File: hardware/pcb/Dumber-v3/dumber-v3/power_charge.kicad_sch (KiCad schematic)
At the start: 44 parts, among them P1 USB_C_Plug_GCT_USB4125, Q1 PMN52XP, SW1 SW_Push, U3 LTC2954, U4 L6924U, U5 NCV5171, U6 DIO6010

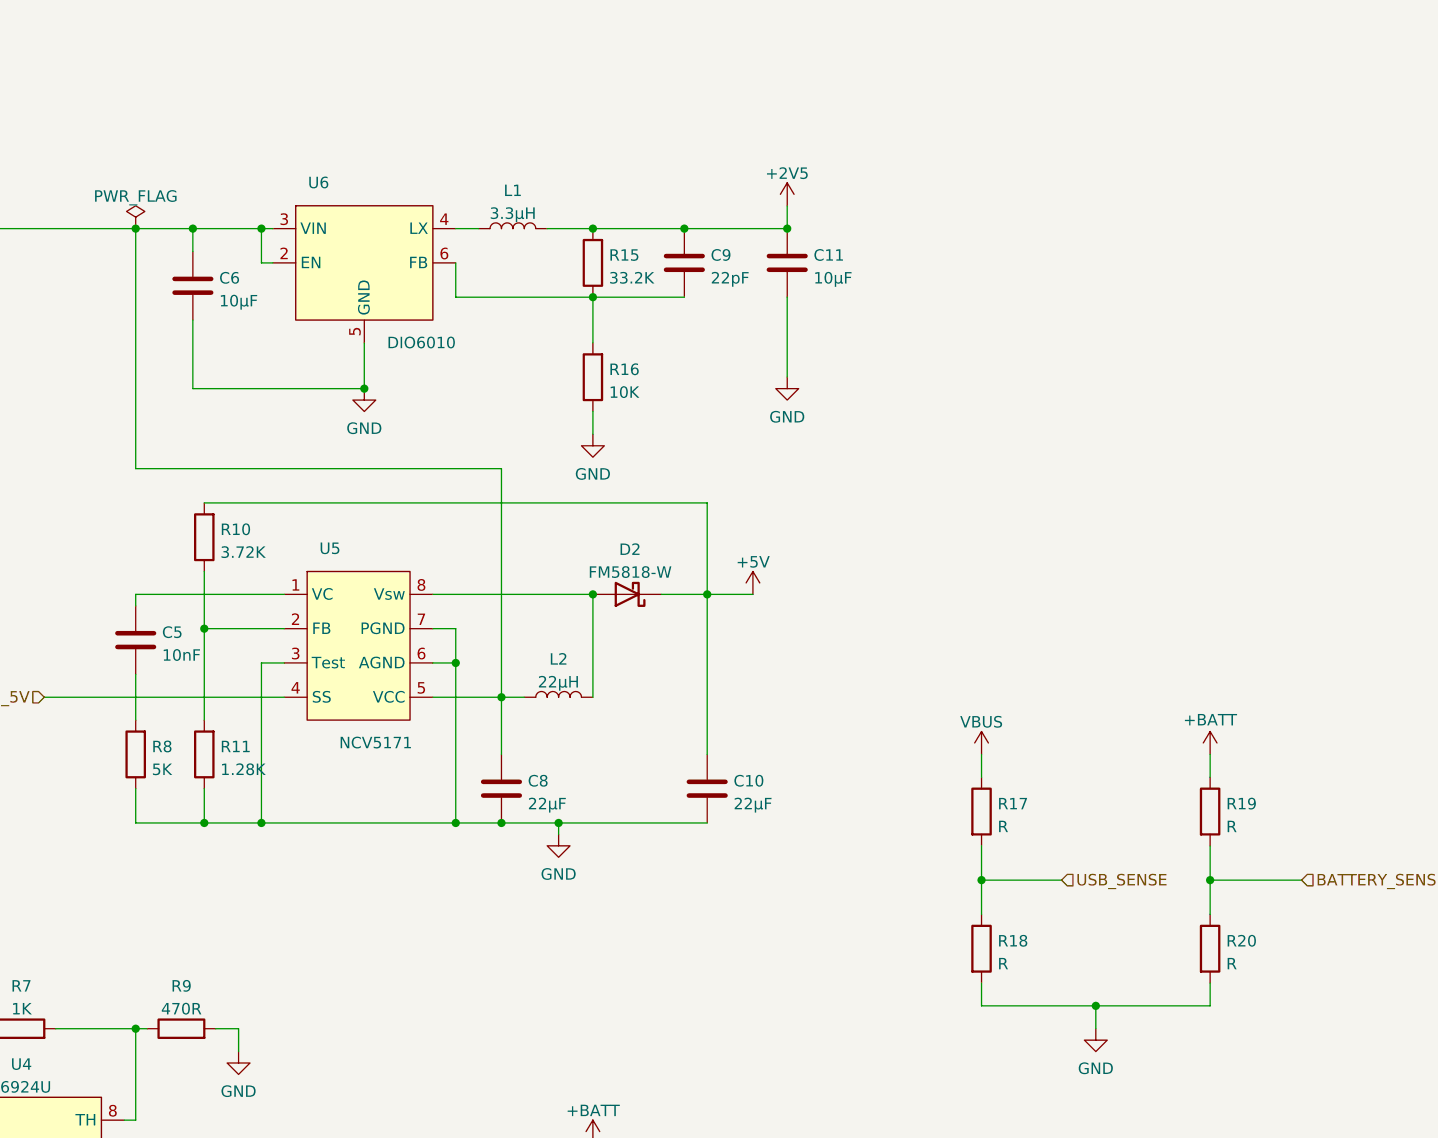
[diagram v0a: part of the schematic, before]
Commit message: Schema complet, projet logiciel demarré
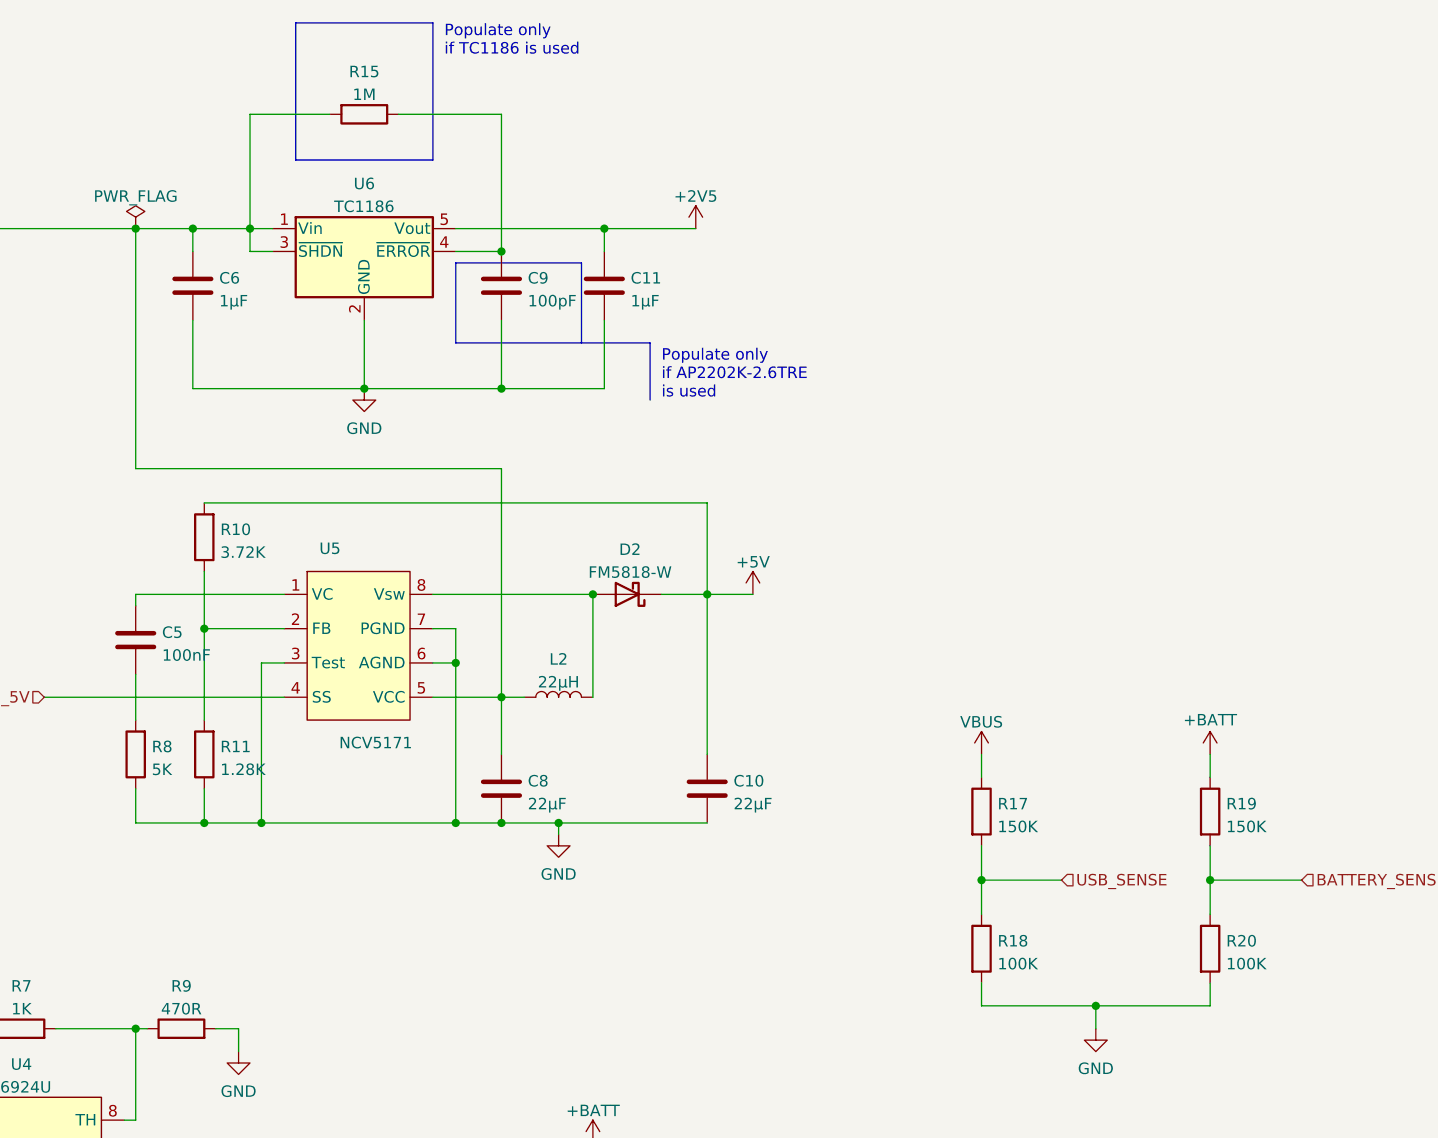
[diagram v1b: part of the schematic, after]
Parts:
- removed L1: 3.3µH, Inductor_SMD:L_Vishay_IHLP-2525, symbol Device:L
- removed R16: 10K, Resistor_SMD:R_0805_2012Metric, symbol Device:R
- removed U6: DIO6010, Package_DFN_QFN:DFN-6-1EP_2x2mm_P0.5mm_EP0.6x1.37mm, symbol Insa:DIO6010
- added U6: TC1186, Package_TO_SOT_SMD:SOT-23-5, symbol Regulator_Linear:TC1186
- C11, C6: value 10µF -> 1µF
- C5: value 10nF -> 100nF
- C9: value 22pF -> 100pF
- L2: footprint Inductor_SMD:L_Vishay_IHLP-4040 -> Inductor_SMD:L_Taiyo-Yuden_MD-4040
- R15: value 33.2K -> 1M
- R17, R19: value R -> 150K
- R18, R20: value R -> 100K
- U4: footprint Package_DFN_QFN:VQFN-16-1EP_3x3mm_P0.5mm_EP1.6x1.6mm_ThermalVias -> INSA:L6924UTR
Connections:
- net +2V5: now also U6.5 (Vout); no longer C9.1, R15.2
- net GND: now also C9.2, U6.2 (GND)
- net at R15.1: now also C9.1, U6.4 (~{ERROR}); no longer C9.2
- net at C6.1, C8.1, D1.3 (A)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: now also R15.2, U6.1 (Vin), U6.3 (~{SHDN})
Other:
- note added: "Populate only if AP2202K-2.6TRE is used"
- note added: "Populate only if TC1186 is used"

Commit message: nouvelle version pcb dumber + nouvelle version monietur en QT
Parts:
- BT1: footprint Battery:BatteryHolder_Keystone_2460_1xAA -> INSA:Battery-14500
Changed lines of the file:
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@@
       (effects (font (size 1.27 1.27)) (justify left))
     )
-    (property "Footprint" "Battery:BatteryHolder_Keystone_2460_1xAA" (id 2) (at 171.45 152.146 90)
+    (property "Footprint" "INSA:Battery-14500" (id 2) (at 171.45 152.146 90)
       (effects (font (size 1.27 1.27)) hide)
     )

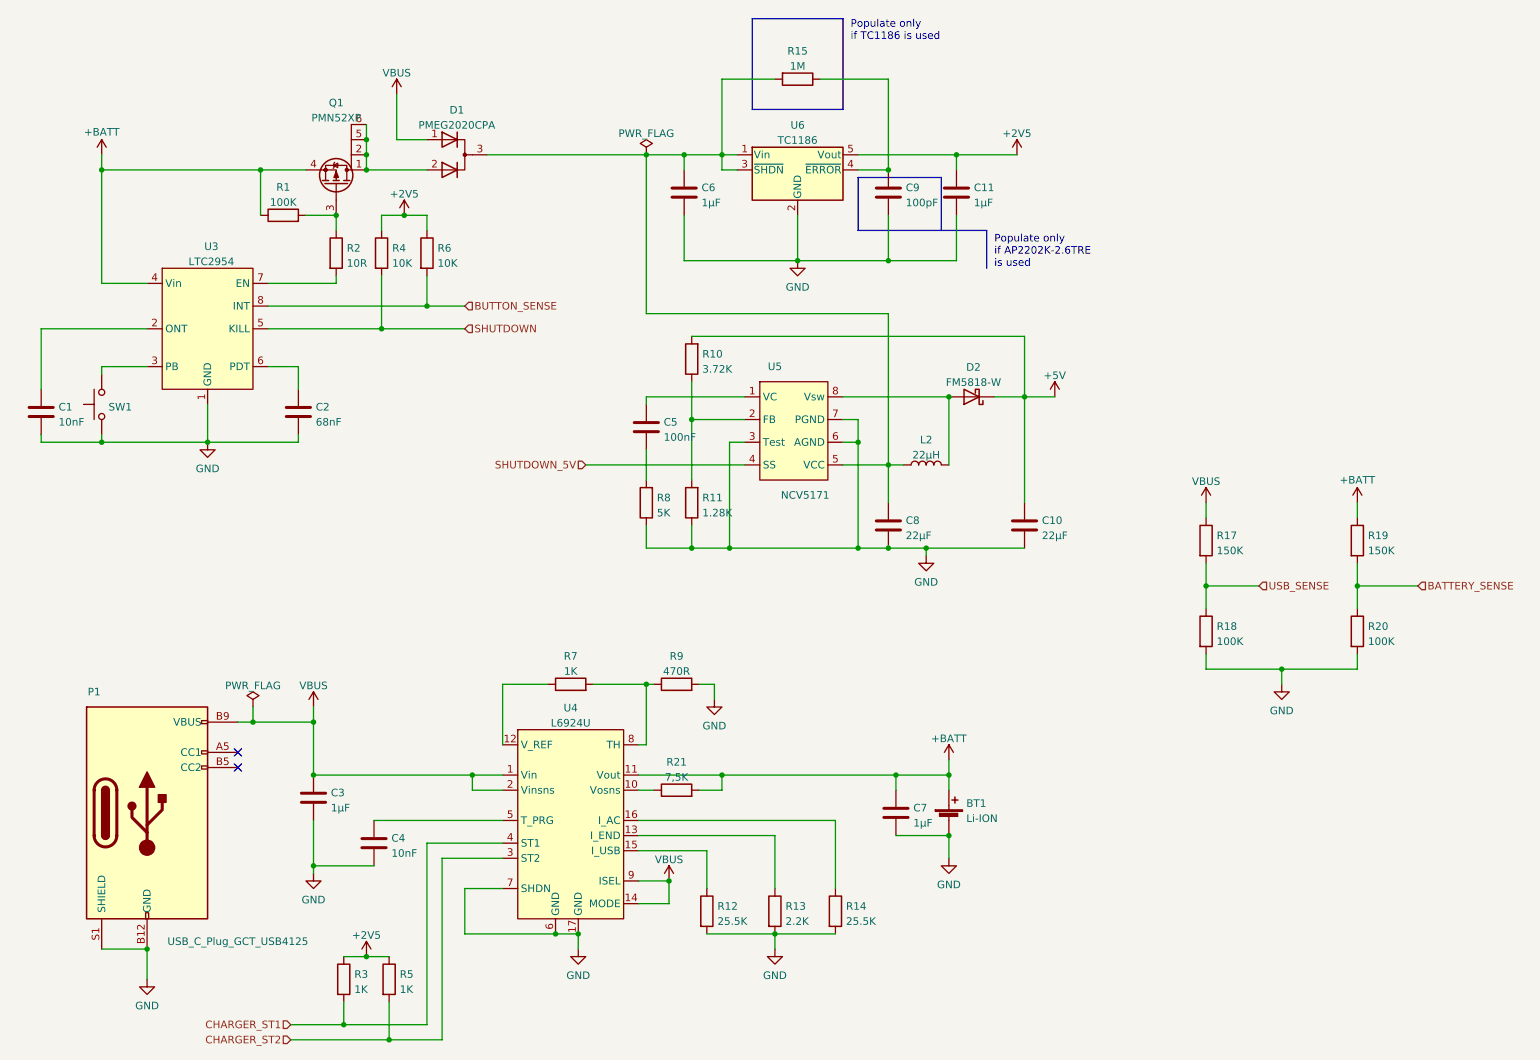
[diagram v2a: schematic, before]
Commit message: Correction de plusieurs erreurs sur la PCB, passé en version 1.1
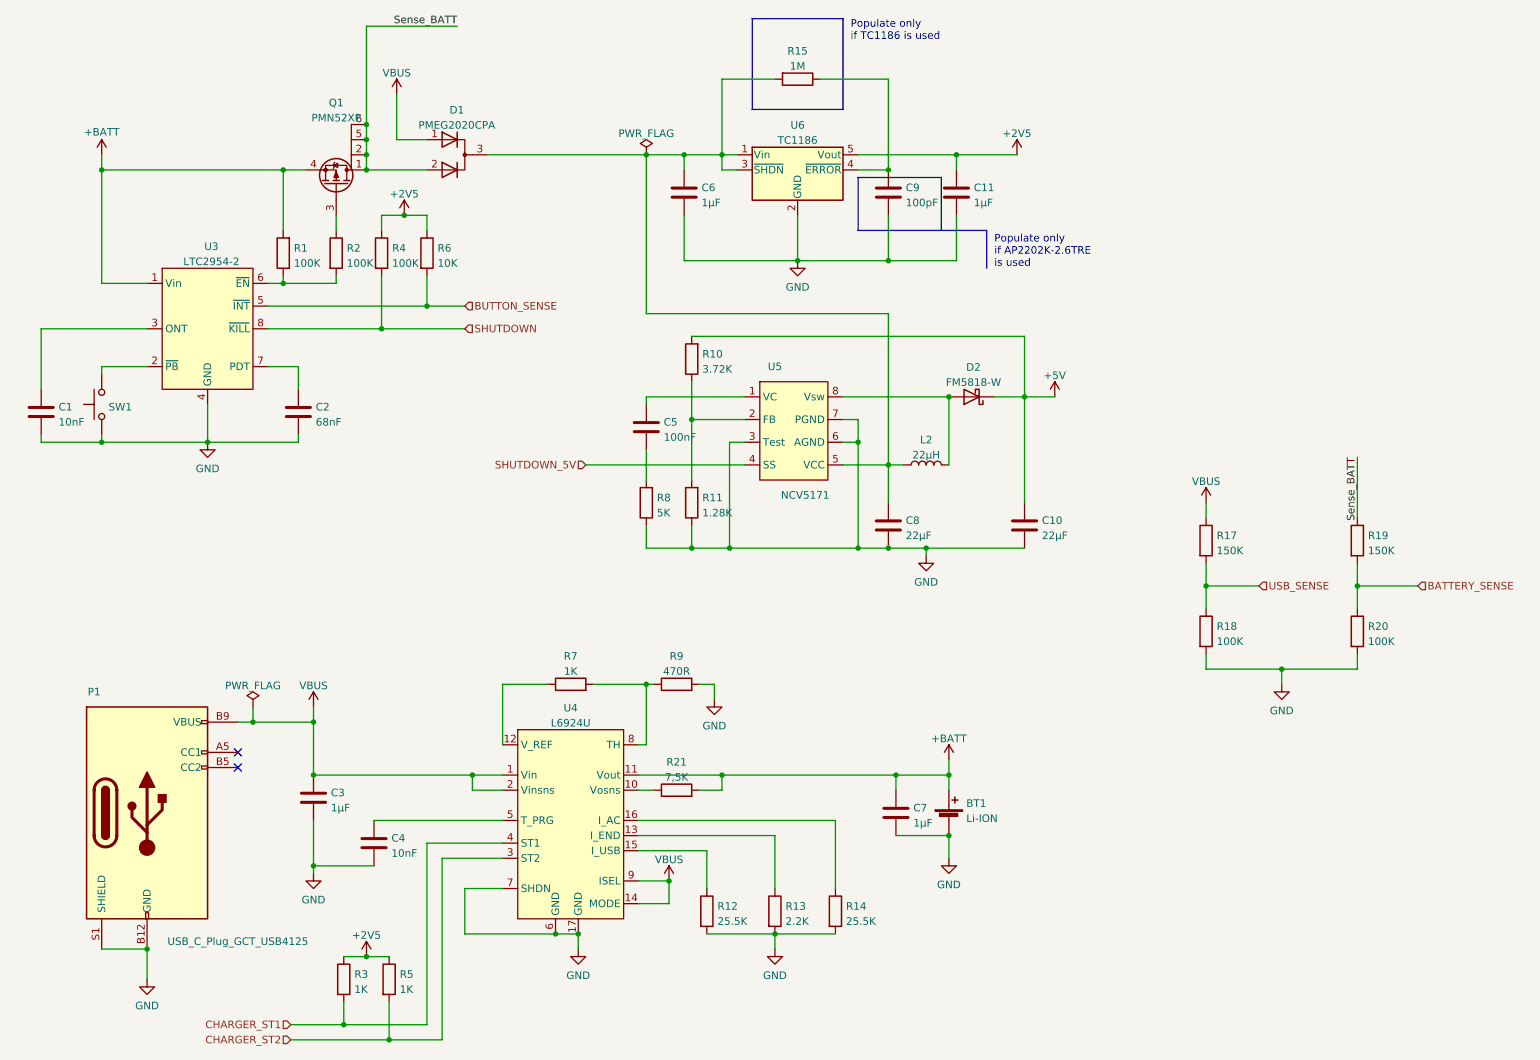
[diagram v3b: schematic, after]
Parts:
- R2: value 10R -> 100K
- R4: value 10K -> 100K
- U3: value LTC2954 -> LTC2954-2
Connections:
- net +BATT: now also R1.2, U3.1 (Vin); no longer R1.1, R19.1, U3.4 (Vin)
- net BUTTON_SENSE: now also U3.5 (~{INT}); no longer U3.8 (INT)
- net GND: now also U3.4 (GND); no longer U3.1 (GND)
- net SHUTDOWN: now also U3.8 (~{KILL}); no longer U3.5 (KILL)
- net Sense_BATT: now reaches D1.2 (K), Q1.1 (D), Q1.2 (D), Q1.5 (D), Q1.6 (D)
- net Sense_BATT: now also R19.1
- net at Q1.3 (G), R2.1: no longer R1.2
- net at SW1.2: now also U3.2 (~{PB}); no longer U3.3 (PB)
- net at C1.1: now also U3.3 (ONT); no longer U3.2 (ONT)
- net at U3.6 (~{EN}): now also R1.1, R2.2; no longer C2.1
- net at U3.7 (PDT): now also C2.1; no longer R2.2
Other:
- moved on the sheet: R1
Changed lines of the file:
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@@
     (title "Power & Charge")
     (date "2022-06-08")
-    (rev "1.0")
+    (rev "1.1")
     (company "INSA - GEI")
   )
+  (junction (at 59.69 44.45) (diameter 0) (color 0 0 0 0)
+  )
   (junction (at 214.63 114.3) (diameter 0) (color 0 0 0 0)
   )
@@
   (junction (at 76.2 71.12) (diameter 0) (color 0 0 0 0)
   )
-  (junction (at 55.88 44.45) (diameter 0) (color 0 0 0 0)
+  (junction (at 59.69 63.5) (diameter 0) (color 0 0 0 0)
   )
   (junction (at 161.29 44.45) (diameter 0) (color 0 0 0 0)
@@
   (junction (at 120.65 130.81) (diameter 0) (color 0 0 0 0)
   )
+  (junction (at 73.66 36.83) (diameter 0) (color 0 0 0 0)
+  )
   (junction (at 29.21 44.45) (diameter 0) (color 0 0 0 0)
   )
   (junction (at 105.41 172.72) (diameter 0) (color 0 0 0 0)
-  )
-  (junction (at 68.58 52.07) (diameter 0) (color 0 0 0 0)
   )
   (junction (at 77.47 190.5) (diameter 0) (color 0 0 0 0)
@@
     (stroke (width 0) (type default) (color 0 0 0 0))
   )
+  (wire (pts (xy 59.69 44.45) (xy 59.69 54.61))
+    (stroke (width 0) (type default) (color 0 0 0 0))
+  )
   (wire (pts (xy 69.85 176.53) (xy 73.66 176.53))
     (stroke (width 0) (type default) (color 0 0 0 0))
@@
     (stroke (width 0) (type default) (color 0 0 0 0))
   )
-  (wire (pts (xy 240.03 100.33) (xy 240.03 102.87))
+  (wire (pts (xy 240.03 92.71) (xy 240.03 102.87))
     (stroke (width 0) (type default) (color 0 0 0 0))
   )
@@
     (stroke (width 0) (type default) (color 0 0 0 0))
   )
+  (wire (pts (xy 59.69 62.23) (xy 59.69 63.5))
+    (stroke (width 0) (type default) (color 0 0 0 0))
+  )
   (wire (pts (xy 129.54 130.81) (xy 132.08 130.81))
     (stroke (width 0) (type default) (color 0 0 0 0))
@@
     (stroke (width 0) (type default) (color 0 0 0 0))
   )
+  (wire (pts (xy 59.69 44.45) (xy 63.5 44.45))
+    (stroke (width 0) (type default) (color 0 0 0 0))
+  )
   (wire (pts (xy 120.65 41.91) (xy 127 41.91))
     (stroke (width 0) (type default) (color 0 0 0 0))
@@
     (stroke (width 0) (type default) (color 0 0 0 0))
   )
-  (wire (pts (xy 29.21 44.45) (xy 55.88 44.45))
-    (stroke (width 0) (type default) (color 0 0 0 0))
-  )
   (wire (pts (xy 161.29 93.98) (xy 163.83 93.98))
     (stroke (width 0) (type default) (color 0 0 0 0))
@@
     (stroke (width 0) (type default) (color 0 0 0 0))
   )
+  (wire (pts (xy 73.66 20.32) (xy 88.9 20.32))
+    (stroke (width 0) (type default) (color 0 0 0 0))
+  )
   (wire (pts (xy 64.77 146.05) (xy 91.44 146.05))
     (stroke (width 0) (type default) (color 0 0 0 0))
@@
     (stroke (width 0) (type default) (color 0 0 0 0))
   )
+  (wire (pts (xy 73.66 36.83) (xy 73.66 20.32))
+    (stroke (width 0) (type default) (color 0 0 0 0))
+  )
   (wire (pts (xy 120.65 68.58) (xy 120.65 41.91))
     (stroke (width 0) (type default) (color 0 0 0 0))
@@
     (stroke (width 0) (type default) (color 0 0 0 0))
   )
-  (wire (pts (xy 57.15 63.5) (xy 68.58 63.5))
+  (wire (pts (xy 57.15 63.5) (xy 59.69 63.5))
     (stroke (width 0) (type default) (color 0 0 0 0))
   )
@@
     (stroke (width 0) (type default) (color 0 0 0 0))
   )
-  (wire (pts (xy 55.88 44.45) (xy 63.5 44.45))
+  (wire (pts (xy 29.21 44.45) (xy 59.69 44.45))
     (stroke (width 0) (type default) (color 0 0 0 0))
   )
@@
     (stroke (width 0) (type default) (color 0 0 0 0))
   )
-  (wire (pts (xy 63.5 52.07) (xy 68.58 52.07))
-    (stroke (width 0) (type default) (color 0 0 0 0))
-  )
   (wire (pts (xy 171.45 160.02) (xy 171.45 156.21))
     (stroke (width 0) (type default) (color 0 0 0 0))
@@
     (stroke (width 0) (type default) (color 0 0 0 0))
   )
+  (wire (pts (xy 59.69 63.5) (xy 68.58 63.5))
+    (stroke (width 0) (type default) (color 0 0 0 0))
+  )
   (wire (pts (xy 62.23 90.17) (xy 62.23 88.9))
     (stroke (width 0) (type default) (color 0 0 0 0))
@@
   )
   (wire (pts (xy 127 59.69) (xy 146.05 59.69))
-    (stroke (width 0) (type default) (color 0 0 0 0))
-  )
-  (wire (pts (xy 55.88 44.45) (xy 55.88 52.07))
     (stroke (width 0) (type default) (color 0 0 0 0))
   )
@@
   (text "Populate only \nif TC1186 is used" (at 154.94 22.86 0)
     (effects (font (size 1.27 1.27)) (justify left bottom))
+  )
+  (label "Sense_BATT" (at 88.9 20.32 180)
+    (effects (font (size 1.27 1.27)) (justify right bottom))
+  )
+  (label "Sense_BATT" (at 240.03 92.71 270)
+    (effects (font (size 1.27 1.27)) (justify right bottom))
   )
   (hierarchical_label "SHUTDOWN_5V" (shape input) (at 110.49 93.98 180)
@@
     (pin "1")
   )
-  (symbol (lib_id "power:+BATT") (at 240.03 100.33 0) (unit 1)
-    (in_bom yes) (on_board yes)
-    (property "Reference" "#PWR027" (id 0) (at 240.03 104.14 0)
-      (effects (font (size 1.27 1.27)) hide)
-    )
-    (property "Value" "+BATT" (id 1) (at 240.03 96.52 0))
-    (property "Footprint" "" (id 2) (at 240.03 100.33 0)
-      (effects (font (size 1.27 1.27)) hide)
-    )
-    (property "Datasheet" "" (id 3) (at 240.03 100.33 0)
-      (effects (font (size 1.27 1.27)) hide)
-    )
-    (pin "1")
-  )
   (symbol (lib_id "power:+5V") (at 189.23 82.55 0) (unit 1)
     (in_bom yes) (on_board yes) (fields_autoplaced)
@@
       (effects (font (size 1.27 1.27)) (justify left))
     )
-    (property "Value" "10K" (id 1) (at 77.978 60.1222 0)
+    (property "Value" "100K" (id 1) (at 77.978 60.1222 0)
       (effects (font (size 1.27 1.27)) (justify left))
     )
@@
     (pin "1")
   )
-  (symbol (lib_id "Device:R") (at 59.69 52.07 90) (unit 1)
-    (in_bom yes) (on_board yes) (fields_autoplaced)
-    (property "Reference" "R1" (id 0) (at 59.69 47.3542 90))
-    (property "Value" "100K" (id 1) (at 59.69 49.8911 90))
-    (property "Footprint" "Resistor_SMD:R_0805_2012Metric" (id 2) (at 59.69 53.848 90)
-      (effects (font (size 1.27 1.27)) hide)
-    )
-    (property "Datasheet" "~" (id 3) (at 59.69 52.07 0)
+  (symbol (lib_id "Device:R") (at 59.69 58.42 180) (unit 1)
+    (in_bom yes) (on_board yes) (fields_autoplaced)
+    (property "Reference" "R1" (id 0) (at 61.468 57.5853 0)
+      (effects (font (size 1.27 1.27)) (justify right))
+    )
+    (property "Value" "100K" (id 1) (at 61.468 60.1222 0)
+      (effects (font (size 1.27 1.27)) (justify right))
+    )
+    (property "Footprint" "Resistor_SMD:R_0805_2012Metric" (id 2) (at 61.468 58.42 90)
+      (effects (font (size 1.27 1.27)) hide)
+    )
+    (property "Datasheet" "~" (id 3) (at 59.69 58.42 0)
       (effects (font (size 1.27 1.27)) hide)
     )
@@
     (in_bom yes) (on_board yes) (fields_autoplaced)
     (property "Reference" "U3" (id 0) (at 47.625 57.311 0))
-    (property "Value" "LTC2954" (id 1) (at 47.625 59.8479 0))
+    (property "Value" "LTC2954-2" (id 1) (at 47.625 59.8479 0))
     (property "Footprint" "Package_TO_SOT_SMD:SOT-23-8" (id 2) (at 48.26 95.25 0)
       (effects (font (size 1.27 1.27)) hide)
@@
       (effects (font (size 1.27 1.27)) (justify left))
     )
-    (property "Value" "10R" (id 1) (at 70.358 60.1222 0)
-      (effects (font (size 1.27 1.27)) (justify left))
-    )
+    (property "Value" "100K" (id 1) (at 70.358 60.1222 0)
+      (effects (font (size 1.27 1.27)) (justify left))
+    )
